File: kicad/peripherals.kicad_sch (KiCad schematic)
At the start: 8 parts, among them SW3 ROM control, U25 27256, U26 27256, U27 27256, U42 PAL L8

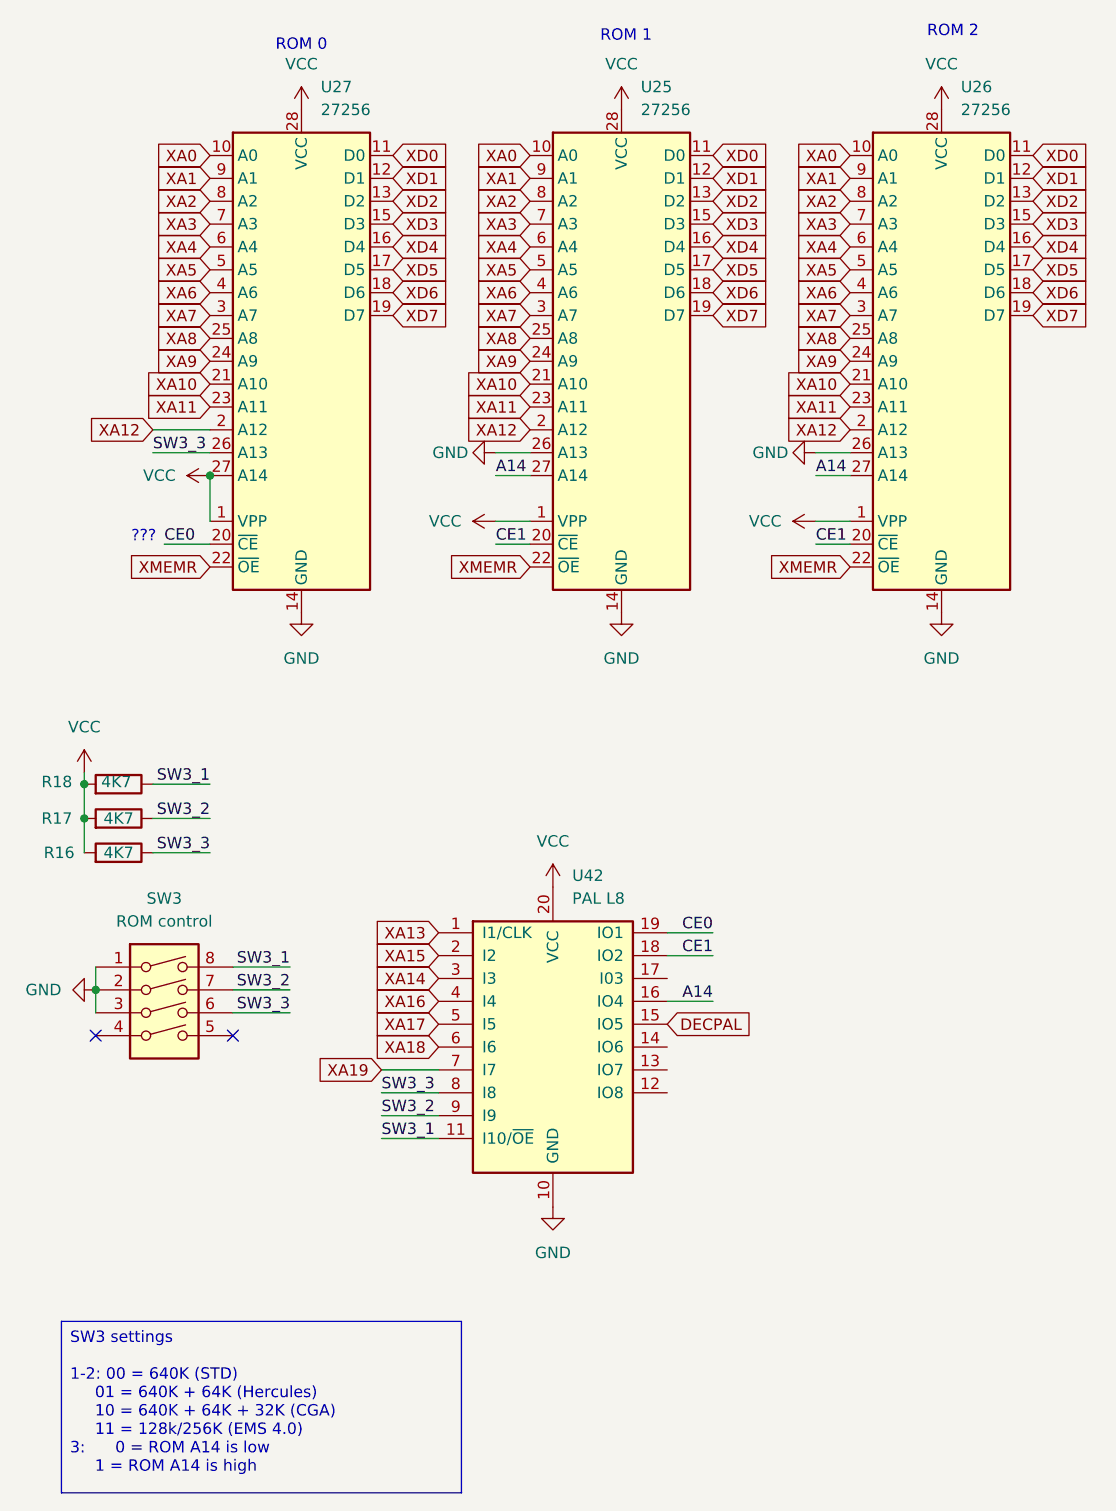
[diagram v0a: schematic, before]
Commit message: finalized schematic
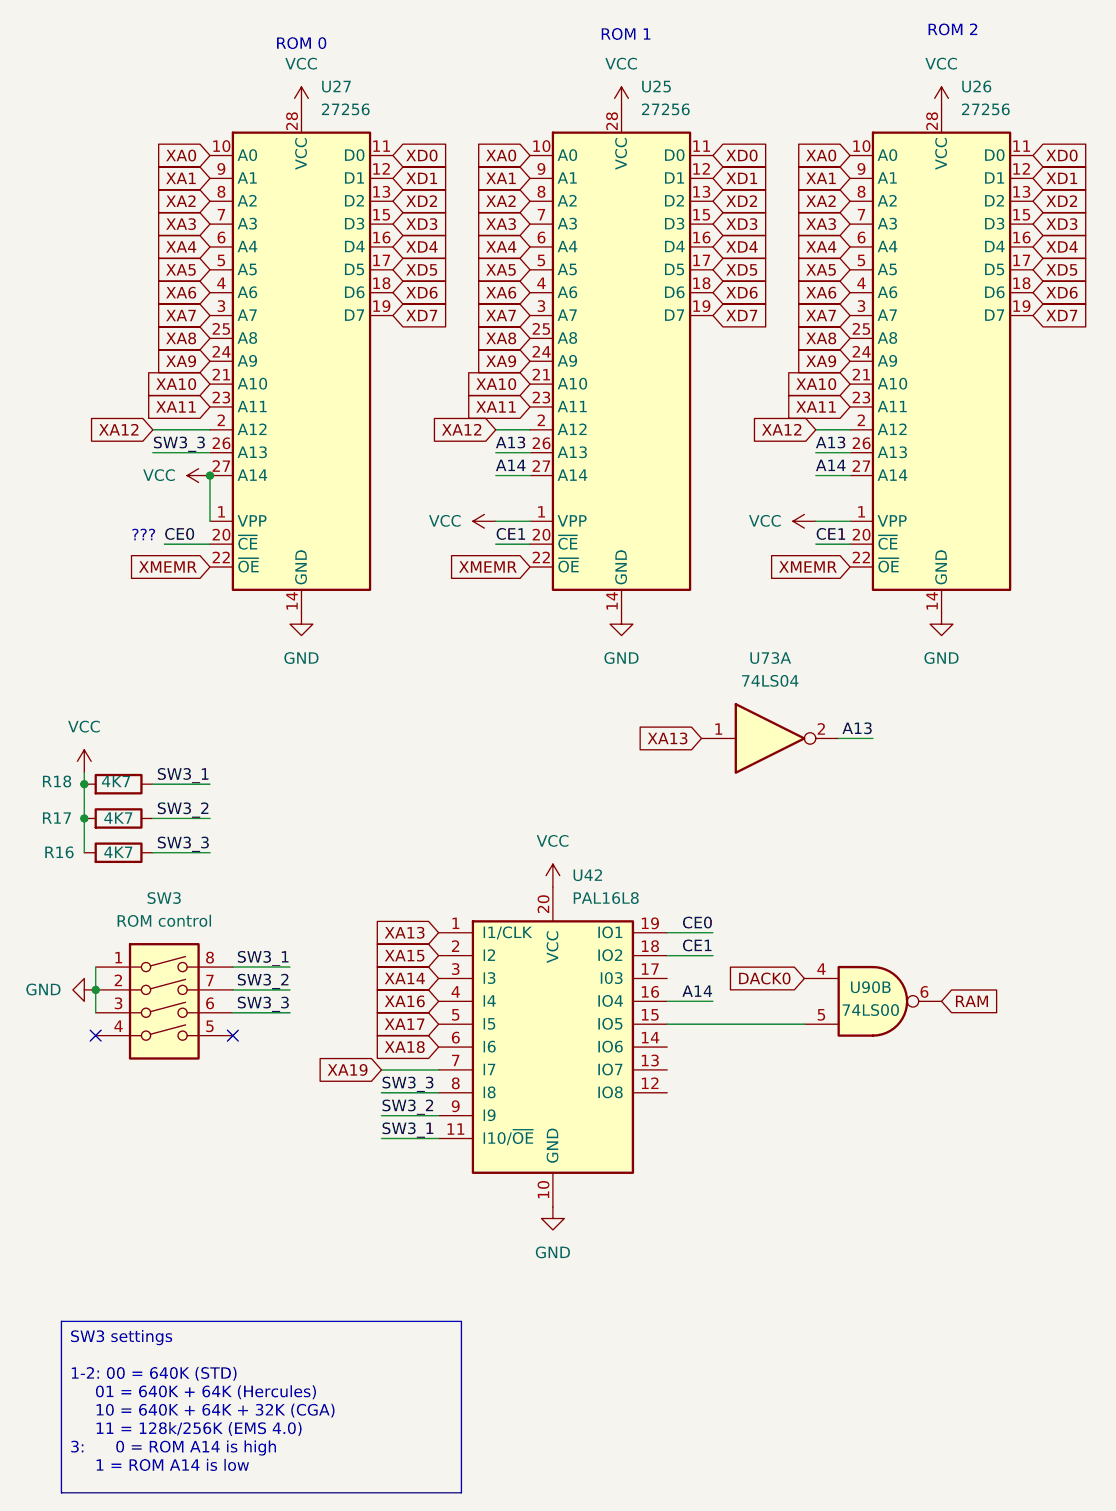
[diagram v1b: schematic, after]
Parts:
- added U73: 74LS04, Package_DIP:DIP-14_W7.62mm, symbol 74xx:74LS04
- added U90: 74LS00, Package_DIP:DIP-14_W7.62mm, symbol 74xx:74LS00
- U42: value PAL L8 -> PAL16L8
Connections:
- net GND: no longer U25.26 (A13), U26.26 (A13)
- net XA13: now also U73.1
- net DECPAL: no longer names the net of U42.15 (IO5)
- net DECPAL: now also U90.5
- new net A13: U25.26 (A13), U26.26 (A13), U73.2
- new net DACK0: U90.4
- new net RAM: U90.6
